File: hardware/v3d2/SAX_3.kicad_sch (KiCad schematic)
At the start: 86 parts, among them J1 joystick, J2 LED strip, J3 SSD1306 SPI, J4 MIDI OUT Y:M5 - R:M4, J5 Batt, J6 Neck - Y:O BK:B R:3.3, J7 Conn_01x03_Female, J8 MXP5010, U1 74HC165, U2 74HC165, U3 74HC165, U4 Teensy3.2_breadboard_friendly

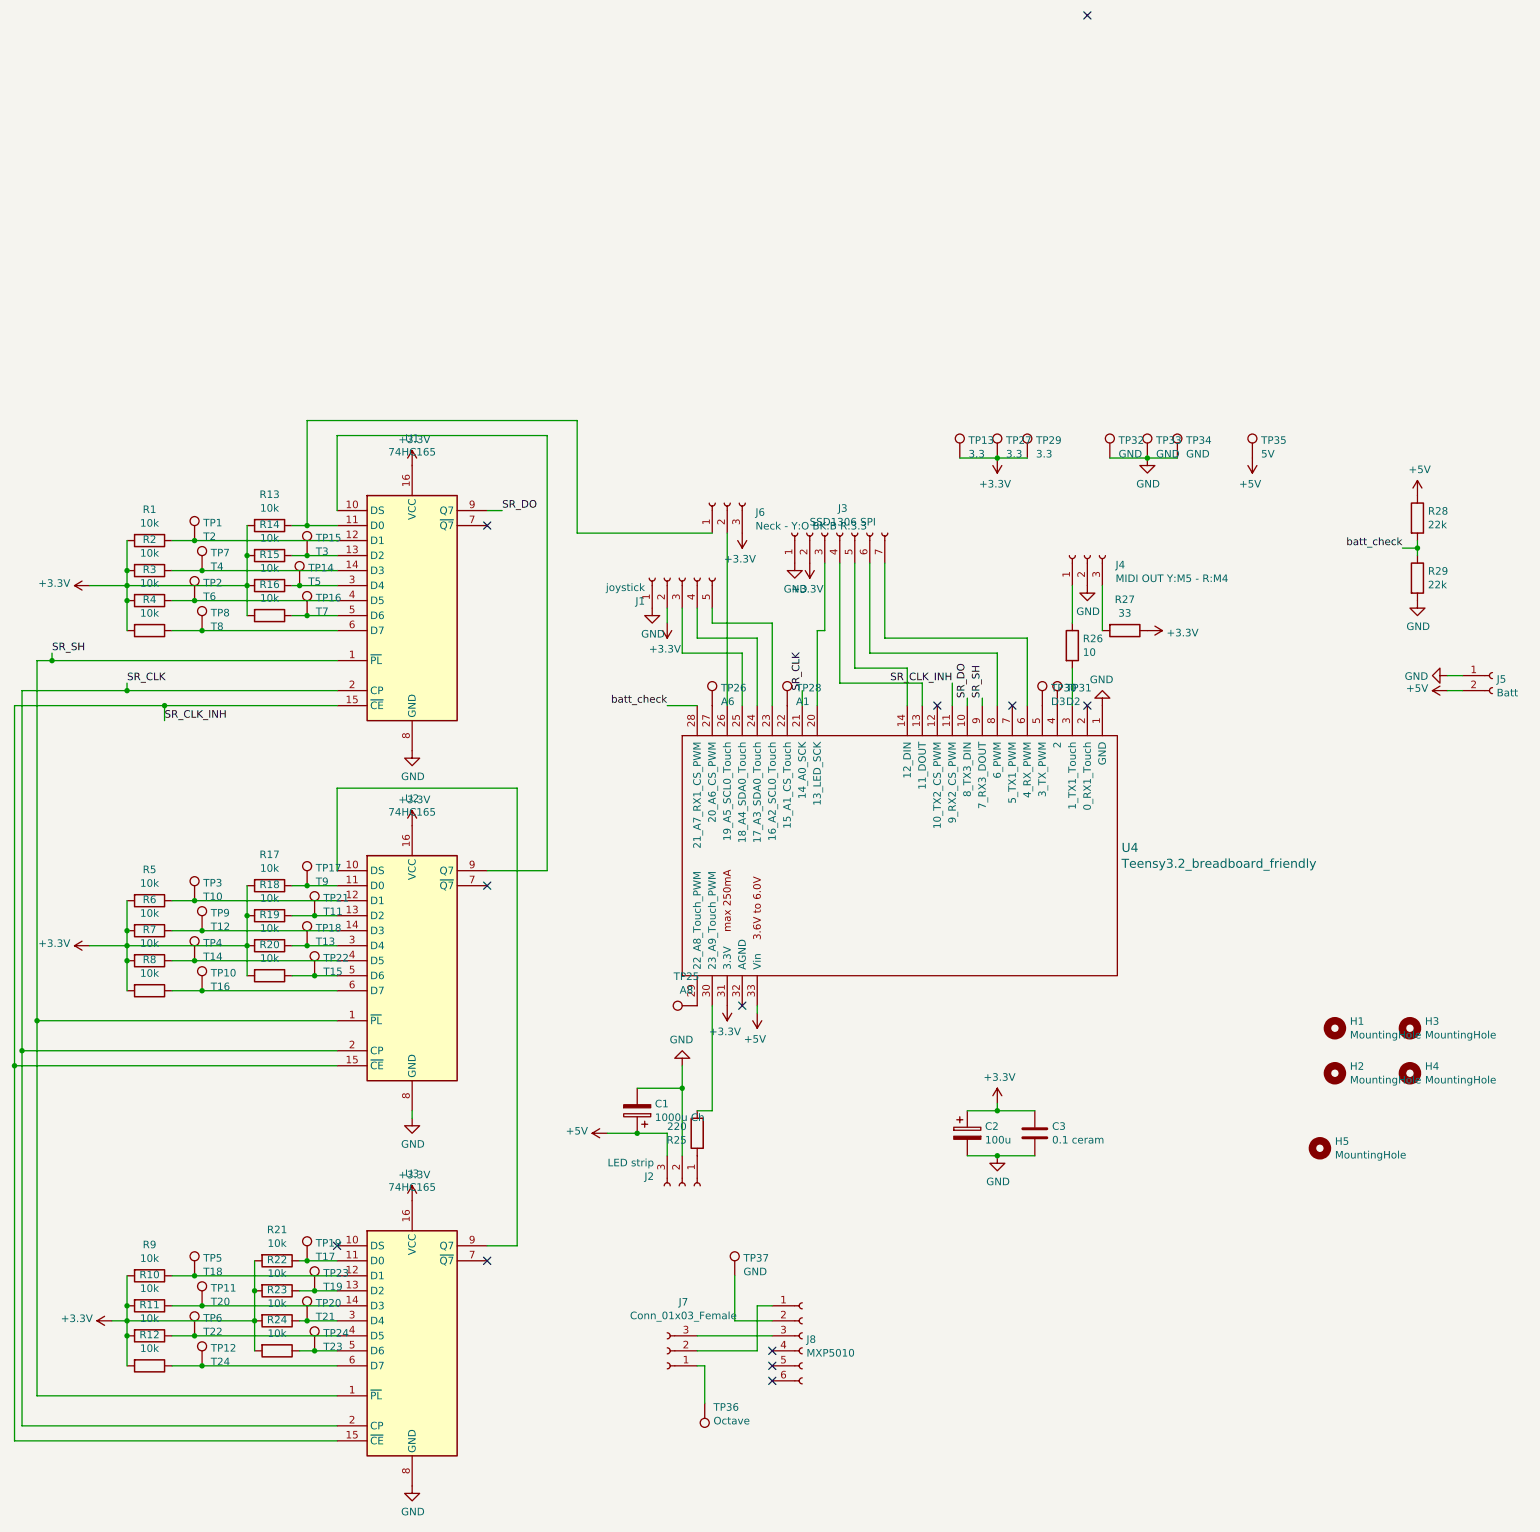
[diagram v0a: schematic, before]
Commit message: Working PCB, improvments on breath input filtering
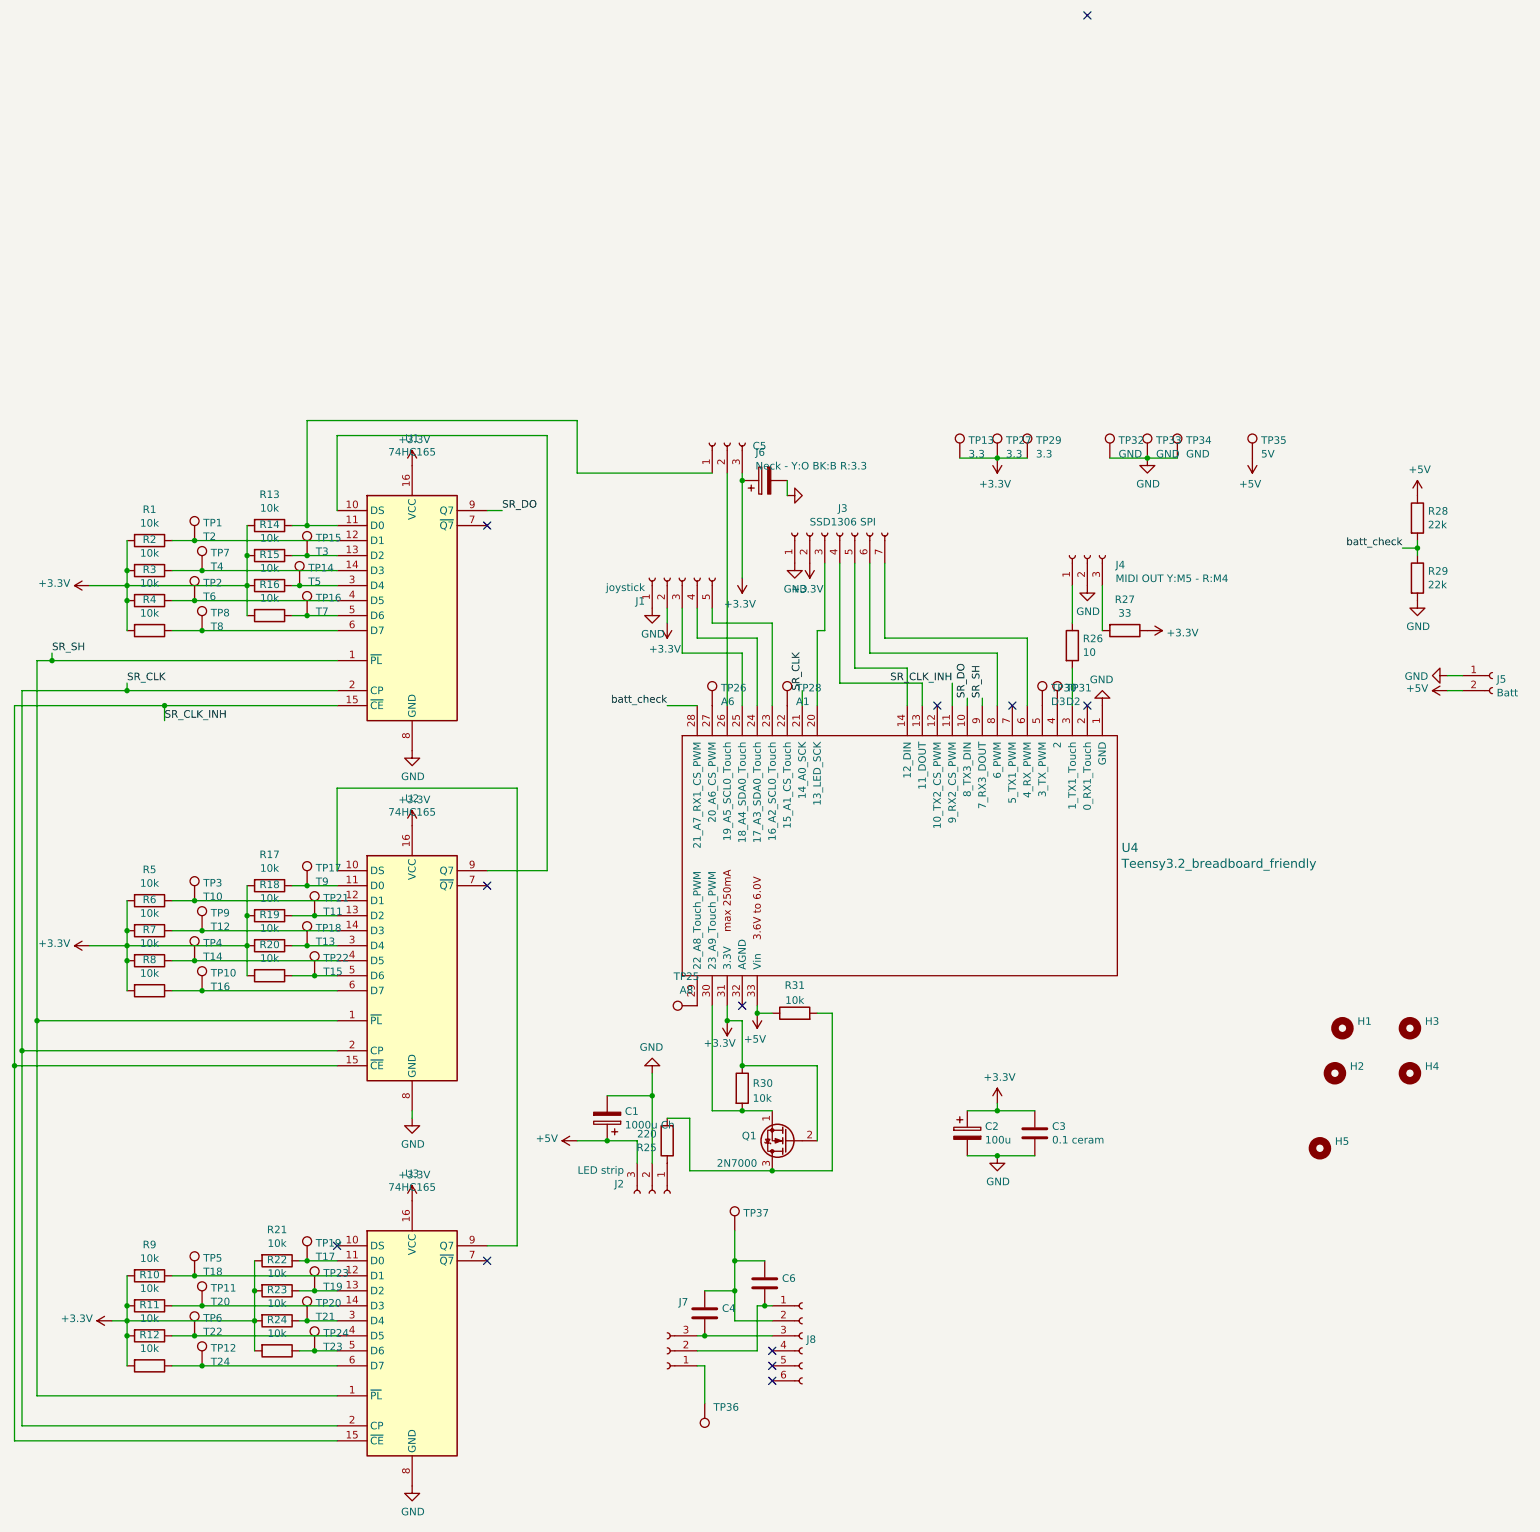
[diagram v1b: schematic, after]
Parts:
- added C4, C6: (no value), symbol Device:C
- added C5: (no value), symbol Device:C_Polarized
- added Q1: 2N7000, Package_TO_SOT_THT:TO-92_HandSolder, symbol Transistor_FET:2N7000
- added R30, R31: 10k, Resistor_THT:R_Axial_DIN0207_L6.3mm_D2.5mm_P7.62mm_Horizontal, symbol Device:R
- C3: footprint Capacitor_THT:C_Axial_L3.8mm_D2.6mm_P7.50mm_Horizontal -> (none)
- H1, H2: value MountingHole -> (none); footprint MountingHole:MountingHole_4.3mm_M4_DIN965_Pad -> (none)
- H3, H4, H5: value MountingHole -> (none); footprint MountingHole:MountingHole_3.2mm_M3_DIN965_Pad -> (none)
- J1: footprint Connector_PinSocket_2.54mm:PinSocket_1x05_P2.54mm_Vertical -> Connector_JST:JST_PH_B5B-PH-K_1x05_P2.00mm_Vertical
- J5: footprint (none) -> Connector_JST:JST_XH_B2B-XH-A_1x02_P2.50mm_Vertical
- J7: value Conn_01x03_Female -> (none); footprint Connector_JST:JST_PH_B3B-PH-K_1x03_P2.00mm_Vertical -> (none)
- J8: value MXP5010 -> (none); footprint Connector_PinSocket_2.54mm:PinSocket_1x06_P2.54mm_Vertical -> (none)
- TP36: value Octave -> (none); footprint TestPoint:TestPoint_THTPad_2.5x2.5mm_Drill1.2mm -> (none)
- TP37: value GND -> (none); footprint TestPoint:TestPoint_THTPad_2.5x2.5mm_Drill1.2mm -> (none)
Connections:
- net +3V3: now also C5.1, Q1.2 (G), R30.1
- net +5V: now also R31.1
- net GND: now also C5.2
- net at U4.30 (23_A9_Touch_PWM): now also Q1.1 (S), R30.2; no longer R25.2
- net at J7.2 (Pin_2), J8.1 (Pin_1): now also C6.2
- net at J8.2 (Pin_2), TP37.1: now also C4.1, C6.1
- net at J7.3 (Pin_3), J8.3 (Pin_3): now also C4.2
- new net: Q1.3 (D), R25.2, R31.2
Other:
- moved on the sheet: C1, H1, J2, J6, R25, TP37
